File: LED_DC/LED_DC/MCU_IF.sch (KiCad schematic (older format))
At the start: 7 parts, among them J1 Conn_01x04, J2 Display Port GPIO, J3 Conn_01x05

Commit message: updated the schematic after feedback.
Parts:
- removed J2: Display Port GPIO, Connector_PinHeader_2.54mm:PinHeader_2x05_P2.54mm_Vertical, symbol Connector_Generic:Conn_02x05_Odd_Even
- removed J3: Conn_01x05, Connector_PinHeader_2.54mm:PinHeader_1x05_P2.54mm_Vertical, symbol Connector_Generic:Conn_01x05
- J1: symbol Connector_Generic:Conn_01x04 -> Connector_Generic:Conn_01x05
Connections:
- net GND: now also J1.5 (Pin_5)
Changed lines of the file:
@@
 Comment4 ""
 $EndDescr
-$Comp
-L Connector_Generic:Conn_02x05_Odd_Even J2
-U 1 1 5FB947BB
-P 2200 4650
-F 0 "J2" H 2250 5067 50  0000 C CNN
-F 1 "Display Port GPIO" H 2250 4976 50  0000 C CNN
-F 2 "Connector_PinHeader_2.54mm:PinHeader_2x05_P2.54mm_Vertical" H 2200 4650 50  0001 C CNN
-F 3 "~" H 2200 4650 50  0001 C CNN
-	1    2200 4650
-	1    0    0    -1
-$EndComp
-$Comp
-L Connector_Generic:Conn_01x05 J3
-U 1 1 5FB95AE3
-P 4300 4600
-F 0 "J3" H 4380 4642 50  0000 L CNN
-F 1 "Conn_01x05" H 4380 4551 50  0000 L CNN
-F 2 "Connector_PinHeader_2.54mm:PinHeader_1x05_P2.54mm_Vertical" H 4300 4600 50  0001 C CNN
-F 3 "~" H 4300 4600 50  0001 C CNN
-	1    4300 4600
-	1    0    0    -1
-$EndComp
-Text GLabel 2000 4550 0    50   Output ~ 0
-D1
-Text GLabel 2000 4650 0    50   Output ~ 0
-D3
-Text GLabel 2000 4750 0    50   Output ~ 0
-D5
-Text GLabel 2000 4850 0    50   Output ~ 0
-D7
-Text GLabel 2500 4450 2    50   Output ~ 0
-D0
-Text GLabel 2500 4550 2    50   Output ~ 0
-D2
-Text GLabel 2500 4650 2    50   Output ~ 0
-D4
-Text GLabel 2500 4750 2    50   Output ~ 0
-D6
-$Comp
-L power:GND #PWR03
-U 1 1 5FB98766
-P 4000 4850
-F 0 "#PWR03" H 4000 4600 50  0001 C CNN
-F 1 "GND" H 4005 4677 50  0000 C CNN
-F 2 "" H 4000 4850 50  0001 C CNN
-F 3 "" H 4000 4850 50  0001 C CNN
-	1    4000 4850
-	1    0    0    -1
-$EndComp
-$Comp
-L power:+5V #PWR06
-U 1 1 5FB9901F
-P 4000 4400
-F 0 "#PWR06" H 4000 4250 50  0001 C CNN
-F 1 "+5V" V 4015 4528 50  0000 L CNN
-F 2 "" H 4000 4400 50  0001 C CNN
-F 3 "" H 4000 4400 50  0001 C CNN
-	1    4000 4400
-	0    -1   -1   0
-$EndComp
-Text GLabel 4000 4600 0    50   Output ~ 0
-C2
-Wire Notes Line
-	5450 4000 5450 5950
-Wire Notes Line
-	5450 5950 1150 5950
-Wire Notes Line
-	1150 5950 1150 4000
-Wire Notes Line
-	1150 4000 5450 4000
-Text GLabel 4000 4500 0    50   Output ~ 0
-C1
-$Comp
-L power:+5V #PWR01
-U 1 1 5FD76D33
-P 1850 4400
-F 0 "#PWR01" H 1850 4250 50  0001 C CNN
-F 1 "+5V" H 1865 4573 50  0000 C CNN
-F 2 "" H 1850 4400 50  0001 C CNN
-F 3 "" H 1850 4400 50  0001 C CNN
-	1    1850 4400
-	1    0    0    -1
-$EndComp
-$Comp
-L power:GND #PWR02
-U 1 1 5FD77C16
-P 2600 4950
-F 0 "#PWR02" H 2600 4700 50  0001 C CNN
-F 1 "GND" H 2605 4777 50  0000 C CNN
-F 2 "" H 2600 4950 50  0001 C CNN
-F 3 "" H 2600 4950 50  0001 C CNN
-	1    2600 4950
-	1    0    0    -1
-$EndComp
-Wire Wire Line
-	2600 4950 2600 4850
-Wire Wire Line
-	2600 4850 2500 4850
-Wire Wire Line
-	1850 4400 1850 4450
-Wire Wire Line
-	1850 4450 2000 4450
-Wire Wire Line
-	4000 4400 4100 4400
-Wire Wire Line
-	4100 4800 4000 4800
-Wire Wire Line
-	4000 4800 4000 4850
-Text GLabel 4000 4700 0    50   Output ~ 0
-C3
-Wire Wire Line
-	4000 4500 4100 4500
-Wire Wire Line
-	4100 4600 4000 4600
-Wire Wire Line
-	4000 4700 4100 4700
-$Comp
-L Connector_Generic:Conn_01x04 J1
-U 1 1 5FEC60A3
-P 7400 4550
-F 0 "J1" H 7480 4542 50  0000 L CNN
-F 1 "Conn_01x04" H 7480 4451 50  0000 L CNN
-F 2 "Connector_PinHeader_2.54mm:PinHeader_1x04_P2.54mm_Vertical" H 7400 4550 50  0001 C CNN
-F 3 "~" H 7400 4550 50  0001 C CNN
-	1    7400 4550
-	1    0    0    -1
-$EndComp
 Text GLabel 6950 4450 0    50   Output ~ 0
 KEY_ROW1
@@
 Wire Wire Line
 	7200 4650 6950 4650
-$Comp
-L power:PWR_FLAG #FLG0101
-U 1 1 5FF0A6FB
-P 1750 4450
-F 0 "#FLG0101" H 1750 4525 50  0001 C CNN
-F 1 "PWR_FLAG" V 1750 4577 50  0000 L CNN
-F 2 "" H 1750 4450 50  0001 C CNN
-F 3 "~" H 1750 4450 50  0001 C CNN
-	1    1750 4450
-	0    -1   -1   0
-$EndComp
-$Comp
-L power:PWR_FLAG #FLG0102
-U 1 1 5FF0AD0F
-P 2700 4850
-F 0 "#FLG0102" H 2700 4925 50  0001 C CNN
-F 1 "PWR_FLAG" V 2700 4978 50  0000 L CNN
-F 2 "" H 2700 4850 50  0001 C CNN
-F 3 "~" H 2700 4850 50  0001 C CNN
-	1    2700 4850
-	0    1    1    0
-$EndComp
-Wire Wire Line
-	2700 4850 2600 4850
-Connection ~ 2600 4850
-Wire Wire Line
-	1750 4450 1850 4450
-Connection ~ 1850 4450
 $Comp
 L Mechanical:MountingHole_Pad H1
@@
 Wire Notes Line
 	8050 1300 9800 1300
+$Comp
+L Connector_Generic:Conn_01x05 J1
+U 1 1 5FEC60A3
+P 7400 4650
+F 0 "J1" H 7480 4642 50  0000 L CNN
+F 1 "Conn_01x04" H 7480 4551 50  0000 L CNN
+F 2 "Connector_PinHeader_2.54mm:PinHeader_1x04_P2.54mm_Vertical" H 7400 4650 50  0001 C CNN
+F 3 "~" H 7400 4650 50  0001 C CNN
+	1    7400 4650
+	1    0    0    -1
+$EndComp
+$Comp
+L power:GND #PWR0101
+U 1 1 6016BEBF
+P 7100 4950
+F 0 "#PWR0101" H 7100 4700 50  0001 C CNN
+F 1 "GND" H 7105 4777 50  0000 C CNN
+F 2 "" H 7100 4950 50  0001 C CNN
+F 3 "" H 7100 4950 50  0001 C CNN
+	1    7100 4950
+	1    0    0    -1
+$EndComp
+Wire Wire Line
+	7100 4950 7100 4850
+Wire Wire Line
+	7100 4850 7200 4850
 $EndSCHEMATC

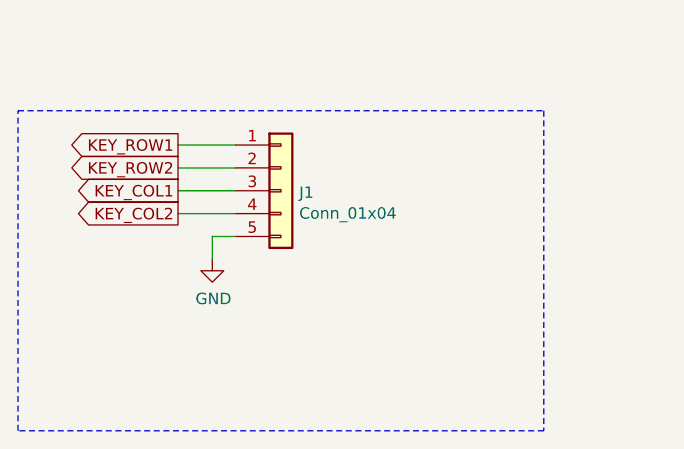
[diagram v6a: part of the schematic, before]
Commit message: Added text to the schematic sections.
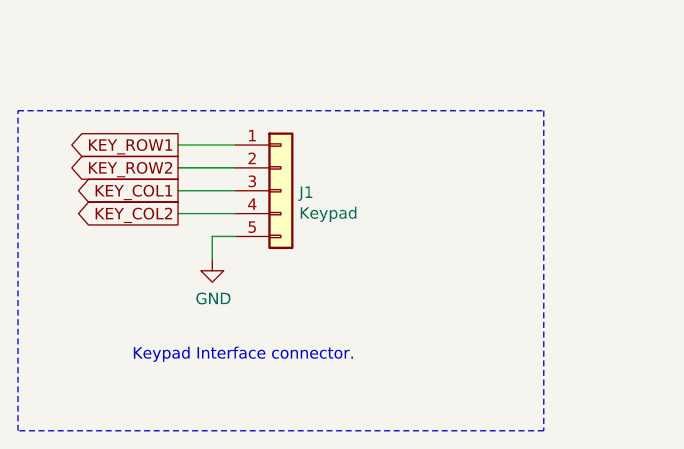
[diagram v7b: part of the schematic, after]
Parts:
- J1: value Conn_01x04 -> Keypad
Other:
- note added: "Keypad Interface connector."
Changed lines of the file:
@@
 P 7400 4650
 F 0 "J1" H 7480 4642 50  0000 L CNN
-F 1 "Conn_01x04" H 7480 4551 50  0000 L CNN
+F 1 "Keypad" H 7480 4551 50  0000 L CNN
 F 2 "Connector_PinHeader_2.54mm:PinHeader_1x04_P2.54mm_Vertical" H 7400 4650 50  0001 C CNN
 F 3 "~" H 7400 4650 50  0001 C CNN
@@
 Wire Wire Line
 	7100 4850 7200 4850
+Text Notes 6750 5400 0    50   ~ 0
+Keypad Interface connector.
 $EndSCHEMATC

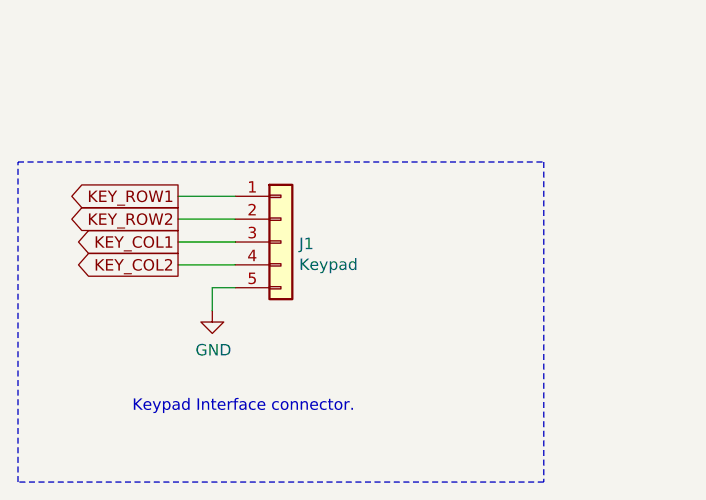
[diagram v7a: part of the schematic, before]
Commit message: Added 20 pin header for MCU LED interface in LED schematic.
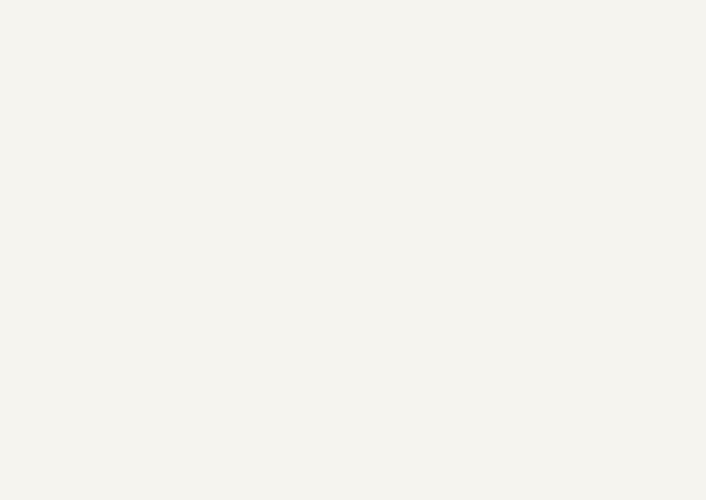
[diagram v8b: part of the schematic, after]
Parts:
- removed J1: Keypad, Connector_PinHeader_2.54mm:PinHeader_1x04_P2.54mm_Vertical, symbol Connector_Generic:Conn_01x05
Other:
- note removed: "Keypad Interface connector."
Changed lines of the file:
@@
 Comment4 ""
 $EndDescr
-Text GLabel 6950 4450 0    50   Output ~ 0
-KEY_ROW1
-Text GLabel 6950 4550 0    50   Output ~ 0
-KEY_ROW2
-Text GLabel 6950 4650 0    50   Output ~ 0
-KEY_COL1
-Text GLabel 6950 4750 0    50   Output ~ 0
-KEY_COL2
-Wire Wire Line
-	6950 4450 7200 4450
-Wire Wire Line
-	7200 4550 6950 4550
-Wire Wire Line
-	7200 4750 6950 4750
-Wire Notes Line
-	8550 4300 8550 5700
-Wire Notes Line
-	8550 5700 6250 5700
-Wire Notes Line
-	6250 5700 6250 4300
-Wire Notes Line
-	6250 4300 8550 4300
-Wire Wire Line
-	7200 4650 6950 4650
 $Comp
 L Mechanical:MountingHole_Pad H1
@@
 Wire Notes Line
 	8050 1300 9800 1300
-$Comp
-L Connector_Generic:Conn_01x05 J1
-U 1 1 5FEC60A3
-P 7400 4650
-F 0 "J1" H 7480 4642 50  0000 L CNN
-F 1 "Keypad" H 7480 4551 50  0000 L CNN
-F 2 "Connector_PinHeader_2.54mm:PinHeader_1x04_P2.54mm_Vertical" H 7400 4650 50  0001 C CNN
-F 3 "~" H 7400 4650 50  0001 C CNN
-	1    7400 4650
-	1    0    0    -1
-$EndComp
-$Comp
-L power:GND #PWR0101
-U 1 1 6016BEBF
-P 7100 4950
-F 0 "#PWR0101" H 7100 4700 50  0001 C CNN
-F 1 "GND" H 7105 4777 50  0000 C CNN
-F 2 "" H 7100 4950 50  0001 C CNN
-F 3 "" H 7100 4950 50  0001 C CNN
-	1    7100 4950
-	1    0    0    -1
-$EndComp
-Wire Wire Line
-	7100 4950 7100 4850
-Wire Wire Line
-	7100 4850 7200 4850
-Text Notes 6750 5400 0    50   ~ 0
-Keypad Interface connector.
 $EndSCHEMATC
